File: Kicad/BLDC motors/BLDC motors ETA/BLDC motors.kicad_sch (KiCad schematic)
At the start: 18 parts, among them U1 ESP32-DEVKIT-V1

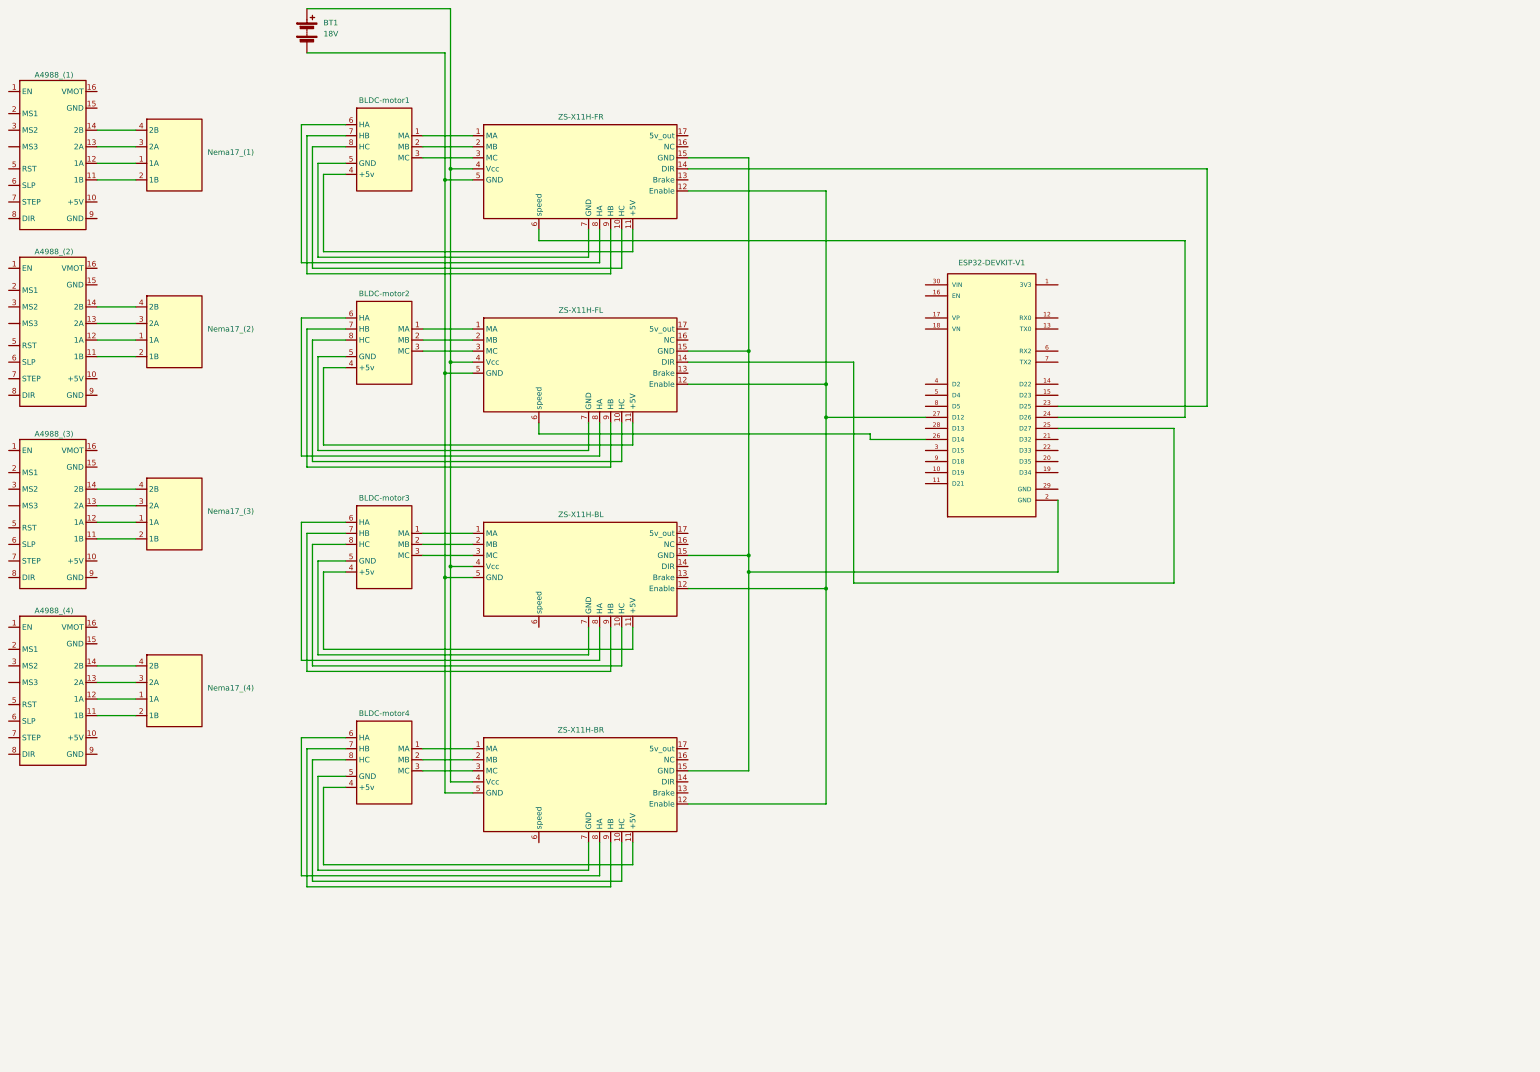
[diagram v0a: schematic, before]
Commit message: added motors
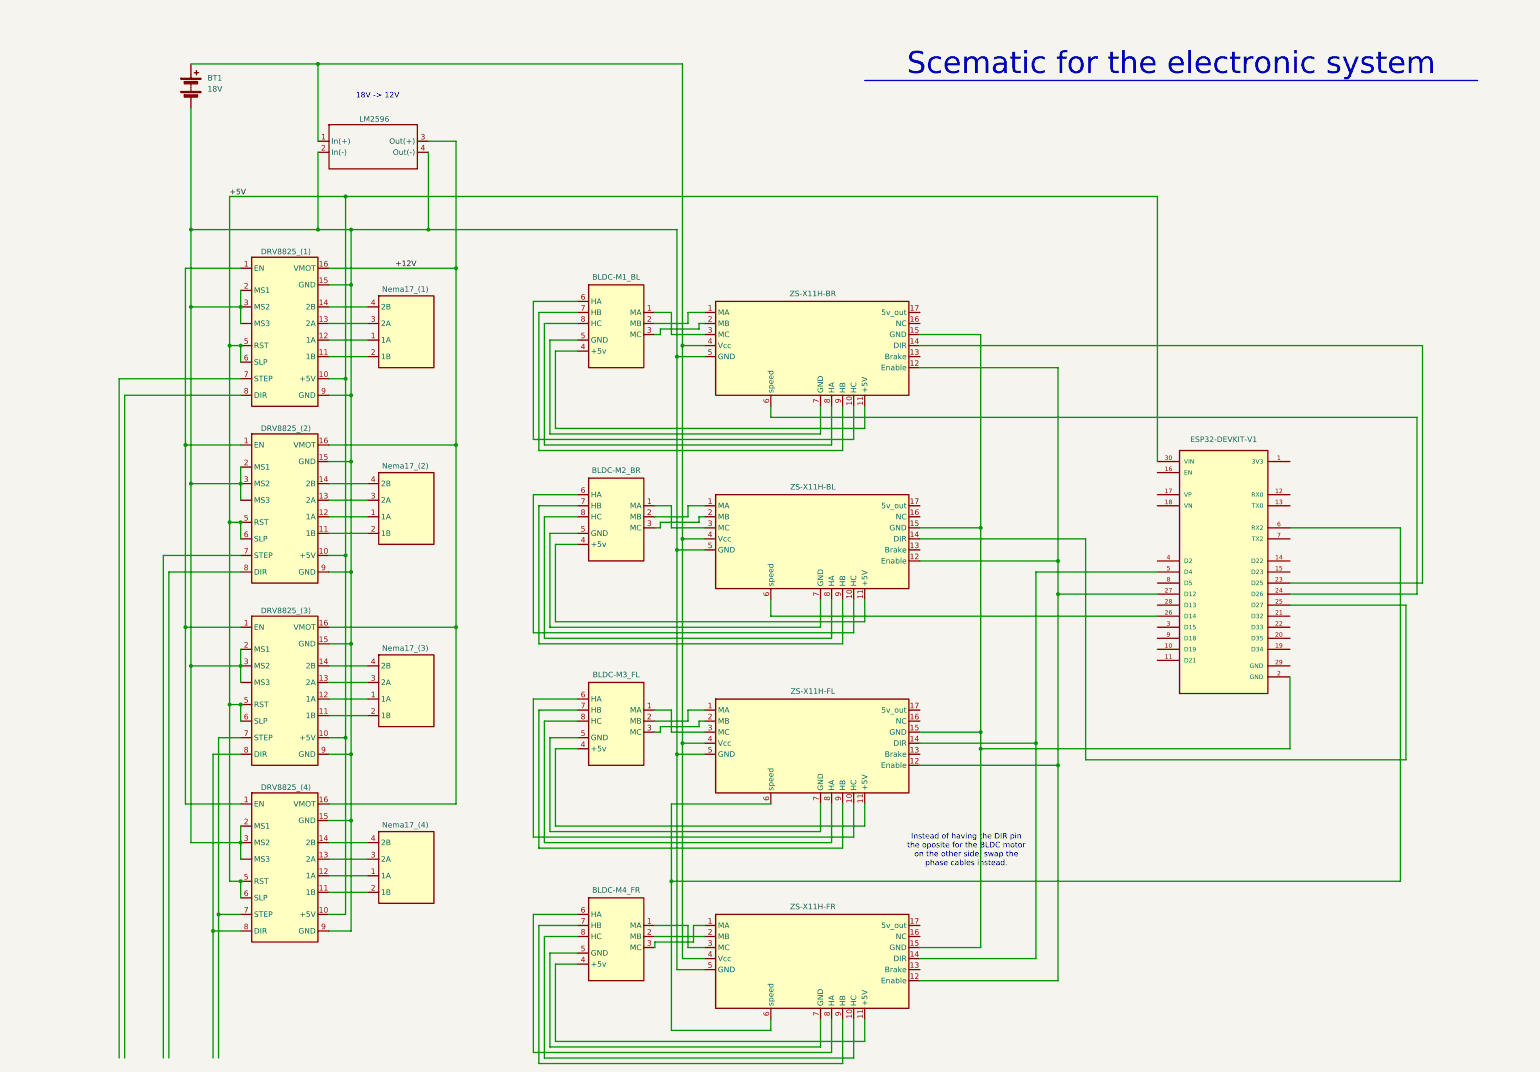
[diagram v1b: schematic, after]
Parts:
- added LM2596: ~, symbol Kandidat:LM2596
- renumbered BLDC-motor1 to BLDC-M1_BL, BLDC-motor2 to BLDC-M2_BR, BLDC-motor3 to BLDC-M3_FL, BLDC-motor4 to BLDC-M4_FR, A4988_(1) to DRV8825_(1), A4988_(2) to DRV8825_(2), A4988_(3) to DRV8825_(3), A4988_(4) to DRV8825_(4), ZS-X11H-FL to ZS-X11H-BL, ZS-X11H-FR to ZS-X11H-BR, ZS-X11H-BL to ZS-X11H-FL, ZS-X11H-BR to ZS-X11H-FR
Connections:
- net at DRV8825_(2). (MS3): now also BT1.2 (-), DRV8825_(1). (MS3), DRV8825_(1).15 (GND), DRV8825_(1).2 (MS1), DRV8825_(1).3 (MS2), DRV8825_(1).9 (GND), DRV8825_(2).15 (GND), DRV8825_(2).2 (MS1), DRV8825_(2).3 (MS2), DRV8825_(2).9 (GND), DRV8825_(3). (MS3), DRV8825_(3).15 (GND), DRV8825_(3).2 (MS1), DRV8825_(3).3 (MS2), DRV8825_(3).9 (GND), DRV8825_(4). (MS3), DRV8825_(4).15 (GND), DRV8825_(4).2 (MS1), DRV8825_(4).3 (MS2), DRV8825_(4).9 (GND), ZS-X11H-BL.5 (GND), ZS-X11H-BR.5 (GND), ZS-X11H-FL.5 (GND), ZS-X11H-FR.5 (GND), LM2596.2 (In(-)), LM2596.4 (Out(-))
- net at DRV8825_(2).1 (EN): now also DRV8825_(1).1 (EN), DRV8825_(3).1 (EN), DRV8825_(4).1 (EN)
- net +5V: now reaches DRV8825_(2).10 (+5V)
- net +5V: now also DRV8825_(1).10 (+5V), DRV8825_(1).5 (RST), DRV8825_(1).6 (SLP), DRV8825_(2).5 (RST), DRV8825_(2).6 (SLP), DRV8825_(3).10 (+5V), DRV8825_(3).5 (RST), DRV8825_(3).6 (SLP), DRV8825_(4).10 (+5V), DRV8825_(4).5 (RST), DRV8825_(4).6 (SLP), U1.30 (VIN)
- net +12V: now reaches DRV8825_(2).16 (VMOT)
- net +12V: now also DRV8825_(1).16 (VMOT), DRV8825_(3).16 (VMOT), DRV8825_(4).16 (VMOT), LM2596.3 (Out(+))
- net at U1.5 (D4): now also ZS-X11H-FL.14 (DIR), ZS-X11H-FR.14 (DIR)
- net at U1.6 (RX2): now also ZS-X11H-FL.6 (speed), ZS-X11H-FR.6 (speed)
- net at DRV8825_(4).7 (STEP): now also DRV8825_(3).7 (STEP)
- net at DRV8825_(4).8 (DIR): now also DRV8825_(3).8 (DIR)
- net at ZS-X11H-FL.1 (MA): now also BLDC-M3_FL.2 (MB); no longer BLDC-M3_FL.1 (MA)
- net at ZS-X11H-FL.10 (HC): now also BLDC-M3_FL.6 (HA); no longer BLDC-M3_FL.8 (HC)
- net at ZS-X11H-FL.2 (MB): now also BLDC-M3_FL.3 (MC); no longer BLDC-M3_FL.2 (MB)
- net at ZS-X11H-FL.3 (MC): now also BLDC-M3_FL.1 (MA); no longer BLDC-M3_FL.3 (MC)
- net at BT1.1 (+), ZS-X11H-BL.4 (Vcc), ZS-X11H-BR.4 (Vcc)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: now also LM2596.1 (In(+))
- net at ZS-X11H-FL.8 (HA): now also BLDC-M3_FL.8 (HC); no longer BLDC-M3_FL.6 (HA)
- net at ZS-X11H-BL.1 (MA): now also BLDC-M2_BR.2 (MB); no longer BLDC-M2_BR.1 (MA)
- net at ZS-X11H-BL.10 (HC): now also BLDC-M2_BR.6 (HA); no longer BLDC-M2_BR.8 (HC)
- net at ZS-X11H-BL.2 (MB): now also BLDC-M2_BR.3 (MC); no longer BLDC-M2_BR.2 (MB)
- net at ZS-X11H-BL.3 (MC): now also BLDC-M2_BR.1 (MA); no longer BLDC-M2_BR.3 (MC)
- net at ZS-X11H-BL.8 (HA): now also BLDC-M2_BR.8 (HC); no longer BLDC-M2_BR.6 (HA)
- net at ZS-X11H-BR.1 (MA): now also BLDC-M1_BL.2 (MB); no longer BLDC-M1_BL.1 (MA)
- net at ZS-X11H-BR.10 (HC): now also BLDC-M1_BL.6 (HA); no longer BLDC-M1_BL.8 (HC)
- net at ZS-X11H-BR.2 (MB): now also BLDC-M1_BL.3 (MC); no longer BLDC-M1_BL.2 (MB)
- net at ZS-X11H-BR.3 (MC): now also BLDC-M1_BL.1 (MA); no longer BLDC-M1_BL.3 (MC)
- net at ZS-X11H-BR.8 (HA): now also BLDC-M1_BL.8 (HC); no longer BLDC-M1_BL.6 (HA)
- net at ZS-X11H-FR.1 (MA): now also BLDC-M4_FR.3 (MC); no longer BLDC-M4_FR.1 (MA)
- net at ZS-X11H-FR.3 (MC): now also BLDC-M4_FR.1 (MA); no longer BLDC-M4_FR.3 (MC)
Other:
- note added: "18V -> 12V"
- note added: "Instead of having the DIR pin the oposite for the BLDC motor on the other side, swap the phase cables instead."
- note added: "Scematic for the electronic system"
- moved on the sheet: BLDC-M1_BL, BLDC-M2_BR, BLDC-M3_FL, BLDC-M4_FR, BT1, DRV8825_(1), DRV8825_(2), DRV8825_(3), DRV8825_(4), Nema17_(1), Nema17_(2), Nema17_(3)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
